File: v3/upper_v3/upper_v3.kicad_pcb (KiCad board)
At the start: 2 copper layers, 41.8 x 71.1 mm, 12 parts, among them J1 Conn_01x27, J10 Conn_01x10_Male, J11 Conn_01x10_Male, J12 Conn_01x10_Male, J2 Conn_01x10_Male, J3 Conn_01x06_Female, J4 Conn_01x05_Female, J5 Conn_01x10_Male, J6 Conn_01x10_Male, J7 Conn_01x10_Male, J8 Conn_01x10_Male, J9 Conn_01x10_Male

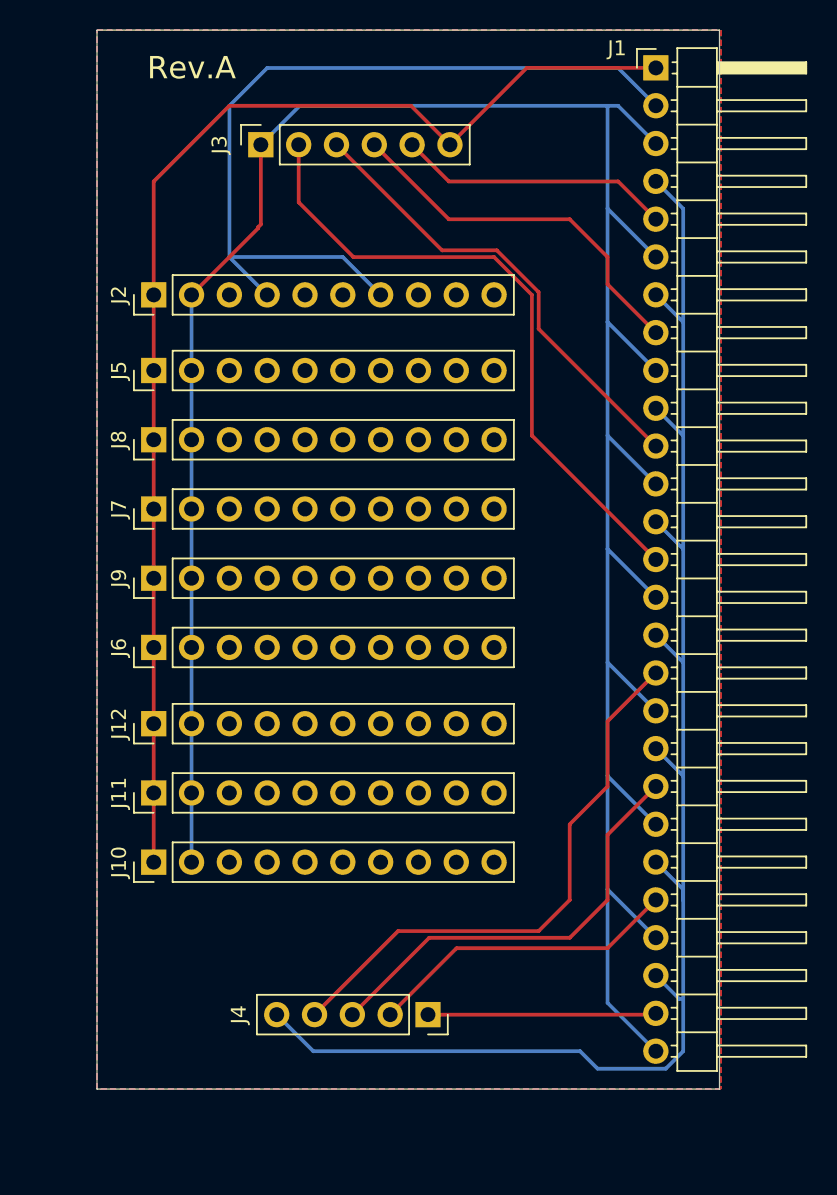
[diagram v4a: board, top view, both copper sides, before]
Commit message: Add pin detail, fixing layout annotation on board
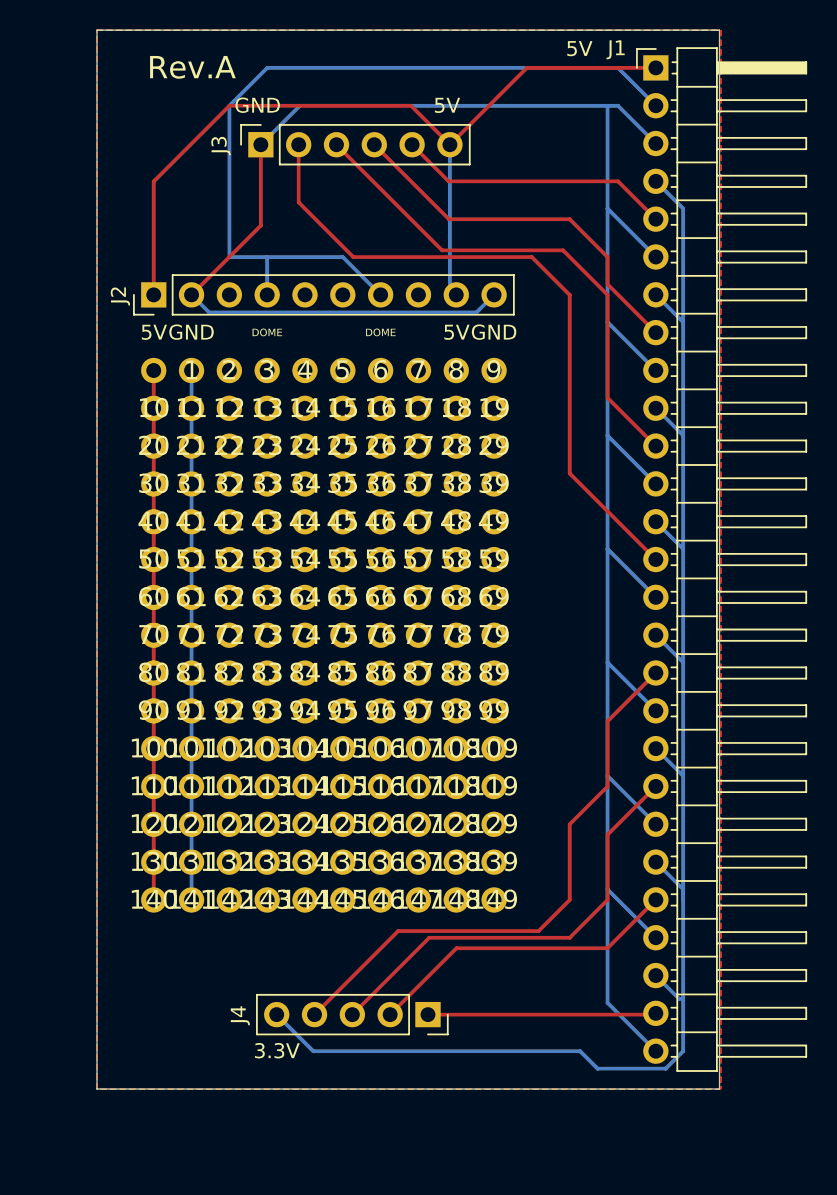
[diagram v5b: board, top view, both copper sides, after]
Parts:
- removed J10, J11, J12, J5, J6, J7, J8, J9: Conn_01x10_Male, Connector_PinHeader_2.54mm:PinHeader_1x10_P2.54mm_Vertical
- added 1: , , F.Cu at (121.9, 78.7)
- added 10: , , F.Cu at (119.4, 81.3)
- added 100: , , F.Cu at (119.4, 104.1)
- added 101: , , F.Cu at (121.9, 104.1)
- added 102: , , F.Cu at (124.5, 104.1)
- added 103: , , F.Cu at (127.0, 104.1)
- added 104: , , F.Cu at (129.5, 104.1)
- added 105: , , F.Cu at (132.1, 104.1)
- added 106: , , F.Cu at (134.6, 104.1)
- added 107: , , F.Cu at (137.2, 104.1)
- added 108: , , F.Cu at (139.7, 104.1)
- added 109: , , F.Cu at (142.2, 104.1)
- added 11: , , F.Cu at (121.9, 81.3)
- added 110: , , F.Cu at (119.4, 106.7)
- added 111: , , F.Cu at (121.9, 106.7)
- added 112: , , F.Cu at (124.5, 106.7)
- added 113: , , F.Cu at (127.0, 106.7)
- added 114: , , F.Cu at (129.5, 106.7)
- added 115: , , F.Cu at (132.1, 106.7)
- added 116: , , F.Cu at (134.6, 106.7)
- added 117: , , F.Cu at (137.2, 106.7)
- added 118: , , F.Cu at (139.7, 106.7)
- added 119: , , F.Cu at (142.2, 106.7)
- added 12: , , F.Cu at (124.5, 81.3)
- added 120: , , F.Cu at (119.4, 109.2)
- added 121: , , F.Cu at (121.9, 109.2)
- added 122: , , F.Cu at (124.5, 109.2)
- added 123: , , F.Cu at (127.0, 109.2)
- added 124: , , F.Cu at (129.5, 109.2)
- added 125: , , F.Cu at (132.1, 109.2)
- added 126: , , F.Cu at (134.6, 109.2)
- added 127: , , F.Cu at (137.2, 109.2)
- added 128: , , F.Cu at (139.7, 109.2)
- added 129: , , F.Cu at (142.2, 109.2)
- added 13: , , F.Cu at (127.0, 81.3)
- added 130: , , F.Cu at (119.4, 111.8)
- added 131: , , F.Cu at (121.9, 111.8)
- added 132: , , F.Cu at (124.5, 111.8)
- added 133: , , F.Cu at (127.0, 111.8)
- added 134: , , F.Cu at (129.5, 111.8)
- added 135: , , F.Cu at (132.1, 111.8)
- added 136: , , F.Cu at (134.6, 111.8)
- added 137: , , F.Cu at (137.2, 111.8)
- added 138: , , F.Cu at (139.7, 111.8)
- added 139: , , F.Cu at (142.2, 111.8)
- added 14: , , F.Cu at (129.5, 81.3)
- added 140: , , F.Cu at (119.4, 114.3)
- added 141: , , F.Cu at (121.9, 114.3)
- added 142: , , F.Cu at (124.5, 114.3)
- added 143: , , F.Cu at (127.0, 114.3)
- added 144: , , F.Cu at (129.5, 114.3)
- added 145: , , F.Cu at (132.1, 114.3)
- added 146: , , F.Cu at (134.6, 114.3)
- added 147: , , F.Cu at (137.2, 114.3)
- added 148: , , F.Cu at (139.7, 114.3)
- added 149: , , F.Cu at (142.2, 114.3)
- added 15: , , F.Cu at (132.1, 81.3)
- added 16: , , F.Cu at (134.6, 81.3)
- added 17: , , F.Cu at (137.2, 81.3)
- added 18: , , F.Cu at (139.7, 81.3)
- added 19: , , F.Cu at (142.2, 81.3)
- added 2: , , F.Cu at (124.5, 78.7)
- added 20: , , F.Cu at (119.4, 83.8)
- added 21: , , F.Cu at (121.9, 83.8)
- added 22: , , F.Cu at (124.5, 83.8)
- added 23: , , F.Cu at (127.0, 83.8)
- added 24: , , F.Cu at (129.5, 83.8)
- added 25: , , F.Cu at (132.1, 83.8)
- added 26: , , F.Cu at (134.6, 83.8)
- added 27: , , F.Cu at (137.2, 83.8)
- added 28: , , F.Cu at (139.7, 83.8)
- added 29: , , F.Cu at (142.2, 83.8)
- added 3: , , F.Cu at (127.0, 78.7)
- added 30: , , F.Cu at (119.4, 86.4)
- added 31: , , F.Cu at (121.9, 86.4)
- added 32: , , F.Cu at (124.5, 86.4)
- added 33: , , F.Cu at (127.0, 86.4)
- added 34: , , F.Cu at (129.5, 86.4)
- added 35: , , F.Cu at (132.1, 86.4)
- added 36: , , F.Cu at (134.6, 86.4)
- added 37: , , F.Cu at (137.2, 86.4)
- added 38: , , F.Cu at (139.7, 86.4)
- added 39: , , F.Cu at (142.2, 86.4)
- added 4: , , F.Cu at (129.5, 78.7)
- added 40: , , F.Cu at (119.4, 88.9)
- added 41: , , F.Cu at (121.9, 88.9)
- added 42: , , F.Cu at (124.5, 88.9)
- added 43: , , F.Cu at (127.0, 88.9)
- added 44: , , F.Cu at (129.5, 88.9)
- added 45: , , F.Cu at (132.1, 88.9)
- added 46: , , F.Cu at (134.6, 88.9)
- added 47: , , F.Cu at (137.2, 88.9)
- added 48: , , F.Cu at (139.7, 88.9)
- added 49: , , F.Cu at (142.2, 88.9)
- added 5: , , F.Cu at (132.1, 78.7)
- added 50: , , F.Cu at (119.4, 91.4)
- added 51: , , F.Cu at (121.9, 91.4)
- added 52: , , F.Cu at (124.5, 91.4)
- added 53: , , F.Cu at (127.0, 91.4)
- added 54: , , F.Cu at (129.5, 91.4)
- added 55: , , F.Cu at (132.1, 91.4)
- added 56: , , F.Cu at (134.6, 91.4)
- added 57: , , F.Cu at (137.2, 91.4)
- added 58: , , F.Cu at (139.7, 91.4)
- added 59: , , F.Cu at (142.2, 91.4)
- added 6: , , F.Cu at (134.6, 78.7)
- added 60: , , F.Cu at (119.4, 94.0)
- added 61: , , F.Cu at (121.9, 94.0)
- added 62: , , F.Cu at (124.5, 94.0)
- added 63: , , F.Cu at (127.0, 94.0)
- added 64: , , F.Cu at (129.5, 94.0)
- added 65: , , F.Cu at (132.1, 94.0)
- added 66: , , F.Cu at (134.6, 94.0)
- added 67: , , F.Cu at (137.2, 94.0)
- added 68: , , F.Cu at (139.7, 94.0)
- added 69: , , F.Cu at (142.2, 94.0)
- added 7: , , F.Cu at (137.2, 78.7)
- added 70: , , F.Cu at (119.4, 96.5)
- added 71: , , F.Cu at (121.9, 96.5)
- added 72: , , F.Cu at (124.5, 96.5)
- added 73: , , F.Cu at (127.0, 96.5)
- added 74: , , F.Cu at (129.5, 96.5)
- added 75: , , F.Cu at (132.1, 96.5)
- added 76: , , F.Cu at (134.6, 96.5)
- added 77: , , F.Cu at (137.2, 96.5)
- added 78: , , F.Cu at (139.7, 96.5)
- added 79: , , F.Cu at (142.2, 96.5)
- added 8: , , F.Cu at (139.7, 78.7)
- added 80: , , F.Cu at (119.4, 99.1)
- added 81: , , F.Cu at (121.9, 99.1)
- added 82: , , F.Cu at (124.5, 99.1)
- added 83: , , F.Cu at (127.0, 99.1)
- added 84: , , F.Cu at (129.5, 99.1)
- added 85: , , F.Cu at (132.1, 99.1)
- added 86: , , F.Cu at (134.6, 99.1)
- added 87: , , F.Cu at (137.2, 99.1)
- added 88: , , F.Cu at (139.7, 99.1)
- added 89: , , F.Cu at (142.2, 99.1)
- added 9: , , F.Cu at (142.2, 78.7)
- added 90: , , F.Cu at (119.4, 101.6)
- added 91: , , F.Cu at (121.9, 101.6)
- added 92: , , F.Cu at (124.5, 101.6)
- added 93: , , F.Cu at (127.0, 101.6)
- added 94: , , F.Cu at (129.5, 101.6)
- added 95: , , F.Cu at (132.1, 101.6)
- added 96: , , F.Cu at (134.6, 101.6)
- added 97: , , F.Cu at (137.2, 101.6)
- added 98: , , F.Cu at (139.7, 101.6)
- added 99: , , F.Cu at (142.2, 101.6)
- added ?: , , F.Cu at (119.4, 78.7)
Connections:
- J2 pad 10: unconnected-(J2-Pad10) -> Net-(J1-Pad12)
- J2 pad 9: unconnected-(J2-Pad9) -> Net-(J1-Pad1)
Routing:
- net unconnected-(J11-Pad10): track 0.00 -> 71.1 mm
- net Net-(J1-Pad1): track 84.8 -> 56.9 mm
- net Net-(J1-Pad12): track 175.7 -> 158.9 mm
- net Net-(J1-Pad11): track 31.3 -> 33.9 mm
- net Net-(J1-Pad14): track 43.3 -> 44.8 mm
- net Net-(J1-Pad2): track 55.7 -> 54.7 mm
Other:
- board text added: "3.3V"
- board text added: "5V"
- board text added: "DOME"
- board text added: "GND"
